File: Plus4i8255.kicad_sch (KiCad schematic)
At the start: 13 parts, among them CN1 EXPANSION_PORT, CN3 PIN_HEADER_32PIN, U1 8255, U2 GAL20V8

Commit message: TurboFloppy -> Plus4i8255
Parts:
- CN1: footprint TurboFloppy:C16_Cart_Conn -> Plus4i8255:C16_Cart_Conn
- V0: footprint TurboFloppy:cc_by_nc_sa -> Plus4i8255:cc_by_nc_sa
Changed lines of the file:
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@@
 			)
 		)
-		(property "Footprint" "TurboFloppy:cc_by_nc_sa"
+		(property "Footprint" "Plus4i8255:cc_by_nc_sa"
 			(at 128.27 193.04 0)
 			(effects
@@
 		)
 		(instances
-			(project "TurboFloppy"
+			(project "Plus4i8255"
 				(path "/0a31112a-e046-4d46-8b9e-0685d05e37f7"
 					(reference "#PWR011")
@@
 		)
 		(instances
-			(project "TurboFloppy"
+			(project "Plus4i8255"
 				(path "/0a31112a-e046-4d46-8b9e-0685d05e37f7"
 					(reference "#PWR026")
@@
 		)
 		(instances
-			(project "TurboFloppy"
+			(project "Plus4i8255"
 				(path "/0a31112a-e046-4d46-8b9e-0685d05e37f7"
 					(reference "#PWR07")
@@
 		)
 		(instances
-			(project "TurboFloppy"
+			(project "Plus4i8255"
 				(path "/0a31112a-e046-4d46-8b9e-0685d05e37f7"
 					(reference "#PWR028")
@@
 		)
 		(instances
-			(project "TurboFloppy"
+			(project "Plus4i8255"
 				(path "/0a31112a-e046-4d46-8b9e-0685d05e37f7"
 					(reference "#PWR023")
@@
 		)
 		(instances
-			(project "TurboFloppy"
+			(project "Plus4i8255"
 				(path "/0a31112a-e046-4d46-8b9e-0685d05e37f7"
 					(reference "#PWR019")
@@
 		)
 		(instances
-			(project "TurboFloppy"
+			(project "Plus4i8255"
 				(path "/0a31112a-e046-4d46-8b9e-0685d05e37f7"
 					(reference "#PWR06")
@@
 		)
 		(instances
-			(project "TurboFloppy"
+			(project "Plus4i8255"
 				(path "/0a31112a-e046-4d46-8b9e-0685d05e37f7"
 					(reference "C2")
@@
 		)
 		(instances
-			(project "TurboFloppy"
+			(project "Plus4i8255"
 				(path "/0a31112a-e046-4d46-8b9e-0685d05e37f7"
 					(reference "#PWR024")
@@
 		)
 		(instances
-			(project "TurboFloppy"
+			(project "Plus4i8255"
 				(path "/0a31112a-e046-4d46-8b9e-0685d05e37f7"
 					(reference "#PWR010")
@@
 		)
 		(instances
-			(project "TurboFloppy"
+			(project "Plus4i8255"
 				(path "/0a31112a-e046-4d46-8b9e-0685d05e37f7"
 					(reference "H2")
@@
 		)
 		(instances
-			(project "TurboFloppy"
+			(project "Plus4i8255"
 				(path "/0a31112a-e046-4d46-8b9e-0685d05e37f7"
 					(reference "#PWR09")
@@
 		)
 		(instances
-			(project "TurboFloppy"
+			(project "Plus4i8255"
 				(path "/0a31112a-e046-4d46-8b9e-0685d05e37f7"
 					(reference "RN3")
@@
 		)
 		(instances
-			(project "TurboFloppy"
+			(project "Plus4i8255"
 				(path "/0a31112a-e046-4d46-8b9e-0685d05e37f7"
 					(reference "RN2")
@@
 		)
 		(instances
-			(project "TurboFloppy"
+			(project "Plus4i8255"
 				(path "/0a31112a-e046-4d46-8b9e-0685d05e37f7"
 					(reference "#PWR04")
@@
 			)
 		)
-		(property "Footprint" "TurboFloppy:C16_Cart_Conn"
+		(property "Footprint" "Plus4i8255:C16_Cart_Conn"
 			(at 52.07 115.57 0)
 			(effects
@@
 		)
 		(instances
-			(project "TurboFloppy"
+			(project "Plus4i8255"
 				(path "/0a31112a-e046-4d46-8b9e-0685d05e37f7"
 					(reference "#PWR025")
@@
 		)
 		(instances
-			(project "TurboFloppy"
+			(project "Plus4i8255"
 				(path "/0a31112a-e046-4d46-8b9e-0685d05e37f7"
 					(reference "#PWR022")
@@
 		)
 		(instances
-			(project "TurboFloppy"
+			(project "Plus4i8255"
 				(path "/0a31112a-e046-4d46-8b9e-0685d05e37f7"
 					(reference "C1")
@@
 		)
 		(instances
-			(project "TurboFloppy"
+			(project "Plus4i8255"
 				(path "/0a31112a-e046-4d46-8b9e-0685d05e37f7"
 					(reference "#PWR03")
@@
 		)
 		(instances
-			(project "TurboFloppy"
+			(project "Plus4i8255"
 				(path "/0a31112a-e046-4d46-8b9e-0685d05e37f7"
 					(reference "#PWR05")
@@
 		)
 		(instances
-			(project "TurboFloppy"
+			(project "Plus4i8255"
 				(path "/0a31112a-e046-4d46-8b9e-0685d05e37f7"
 					(reference "#PWR027")
@@
 		)
 		(instances
-			(project "TurboFloppy"
+			(project "Plus4i8255"
 				(path "/0a31112a-e046-4d46-8b9e-0685d05e37f7"
 					(reference "#PWR020")
@@
 		)
 		(instances
-			(project "TurboFloppy"
+			(project "Plus4i8255"
 				(path "/0a31112a-e046-4d46-8b9e-0685d05e37f7"
 					(reference "#PWR08")

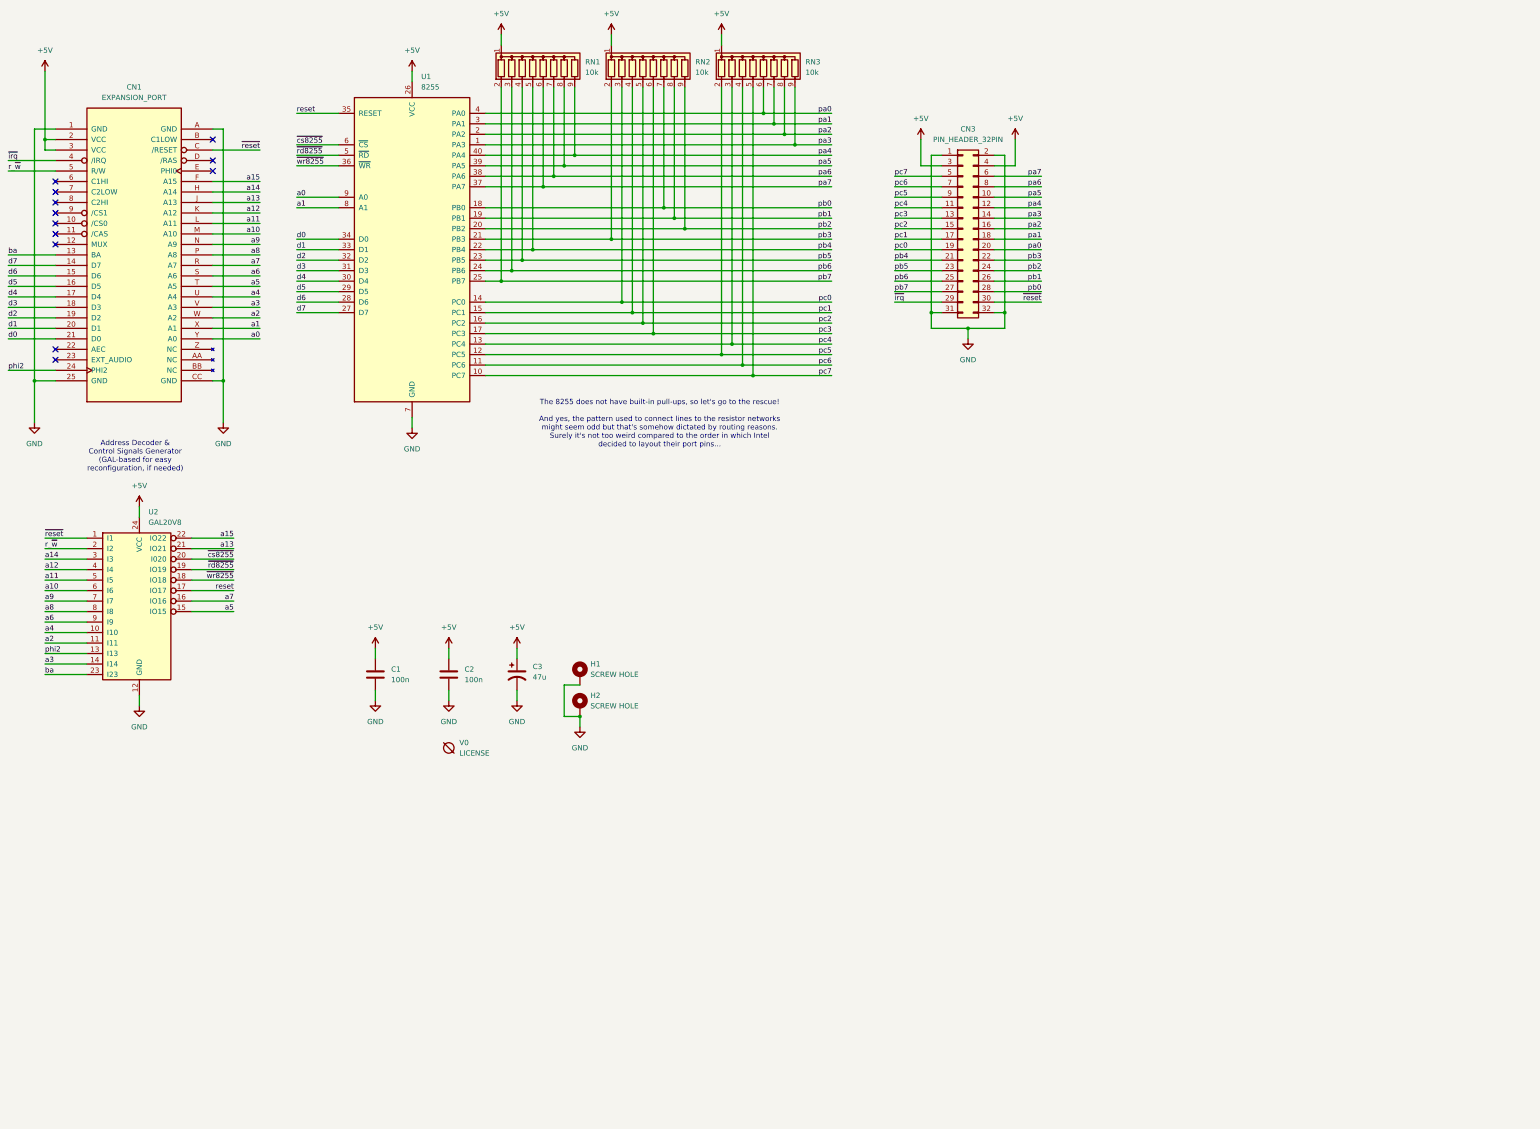
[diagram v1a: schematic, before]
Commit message: Add PC-style DB25 parallel port Inspired by zx_spectrum_parallel_interface by @msolajic TBD: Check DB25 footprint!
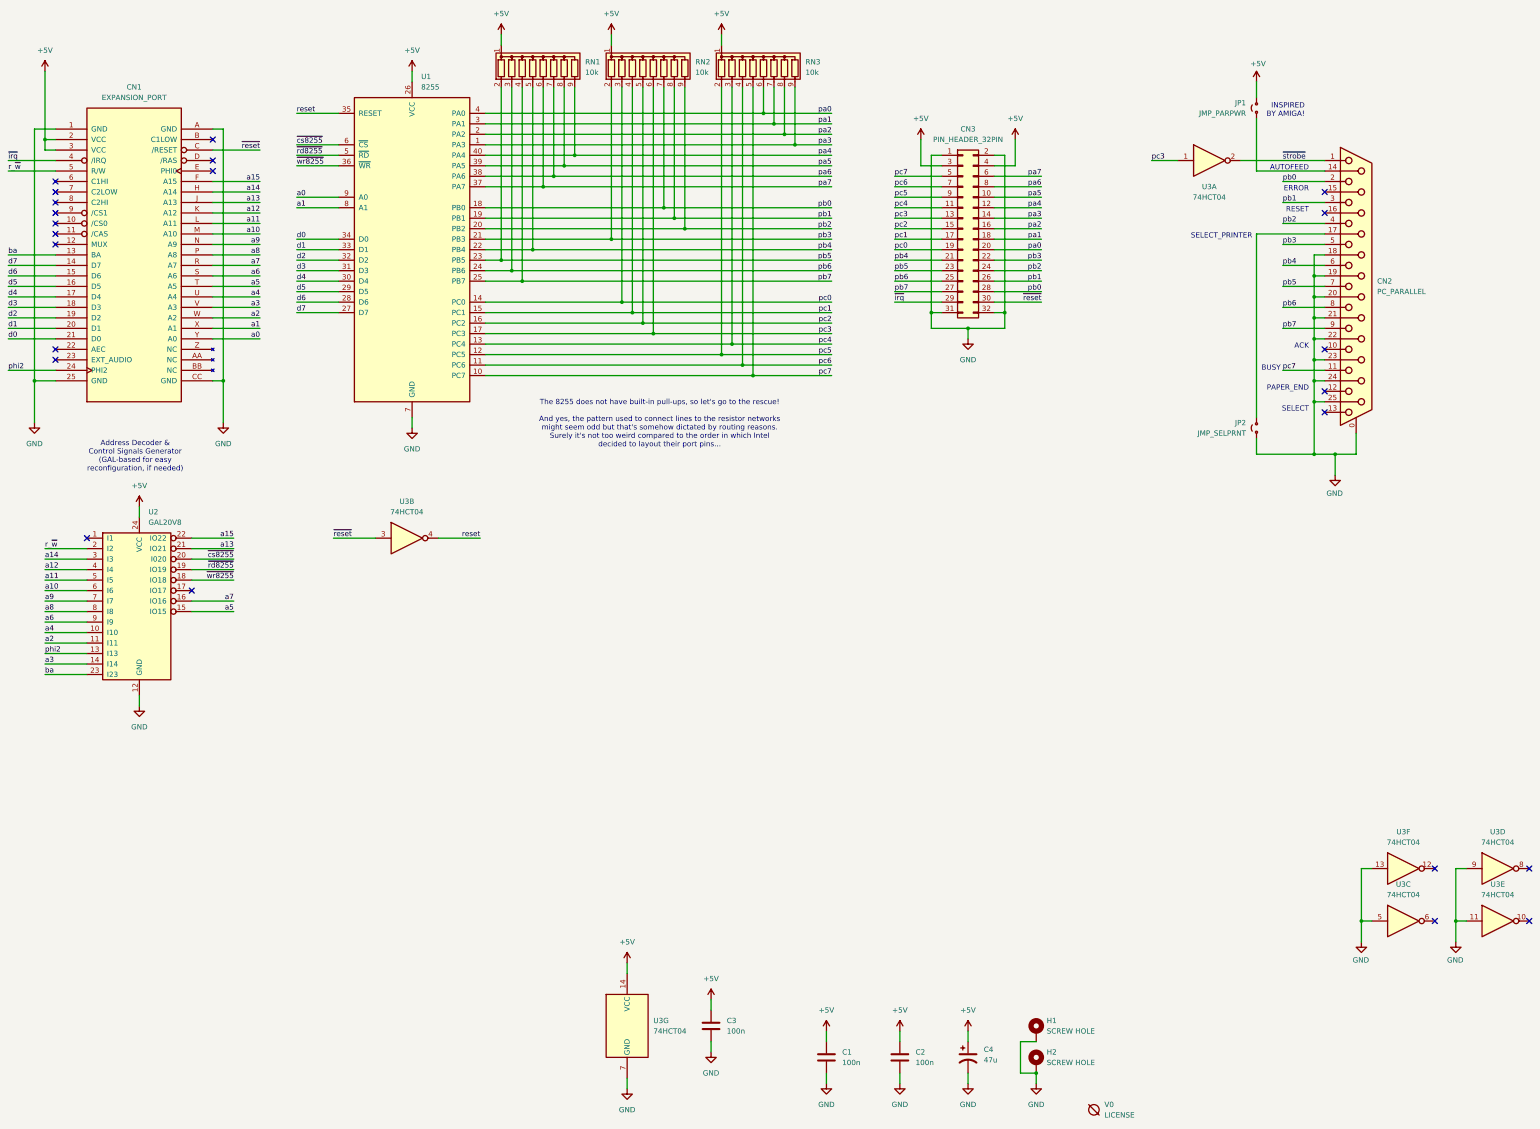
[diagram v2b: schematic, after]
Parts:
- added C3: 100n, Capacitor_THT:C_Disc_D7.0mm_W2.5mm_P5.00mm, symbol Device:C
- added CN2: PC_PARALLEL, Connector_Dsub:DSUB-25_Female_Horizontal_P2.77x2.84mm_EdgePinOffset7.70mm_Housed_MountingHolesOffset9.12mm, symbol Connector:DB25_Receptacle_MountingHoles
- added JP1: JMP_PARPWR, Jumper:SolderJumper-2_P1.3mm_Open_RoundedPad1.0x1.5mm, symbol Jumper:Jumper_2_Small_Open
- added JP2: JMP_SELPRNT, Jumper:SolderJumper-2_P1.3mm_Open_RoundedPad1.0x1.5mm, symbol Jumper:Jumper_2_Small_Open
- added U3: 74HCT04, Package_DIP:DIP-14_W7.62mm_Socket_LongPads, symbol 74xx:74HCT04
- renumbered C3 to C4
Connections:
- net +5V: now also C3.1, JP1.2 (B), U3.14 (VCC)
- net GND: now also C3.2, CN2.0 (PAD), CN2.18 (P18), CN2.19 (P19), CN2.20 (P20), CN2.21 (P21), CN2.22 (P22), CN2.23 (P23), CN2.24 (P24), CN2.25 (P25), JP2.1 (A), U3.11, U3.13, U3.5, U3.7 (GND), U3.9
- net pb0: now also CN2.2
- net pb1: now also CN2.3
- net pb2: now also CN2.4
- net pb3: now also CN2.5
- net pb4: now also CN2.6
- net pb5: now also RN1.2 (R1), CN2.7; no longer RN1.4 (R3)
- net pb6: now also CN2.8
- net pb7: now also RN1.4 (R3), CN2.9; no longer RN1.2 (R1)
- net pc3: now also U3.1
- net pc7: now also CN2.11
- net reset: now also U3.4; no longer U2.17 (IO17)
- net ~{reset}: now also U3.3; no longer U2.1 (I1)
- new net: CN2.17 (P17), JP2.2 (B)
- new net: CN2.14 (P14), JP1.1 (A)
- new net ~{strobe}: CN2.1, U3.2
- no-connect marks 12 -> 23
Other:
- note added: "ACK"
- note added: "AUTOFEED"
- note added: "BUSY"
- note added: "ERROR"
- note added: "INSPIRED BY AMIGA!"
- note added: "PAPER_END"
- note added: "RESET"
- note added: "SELECT"
- note added: "SELECT_PRINTER"
- moved on the sheet: C1, C2, C4, H1, H2, V0

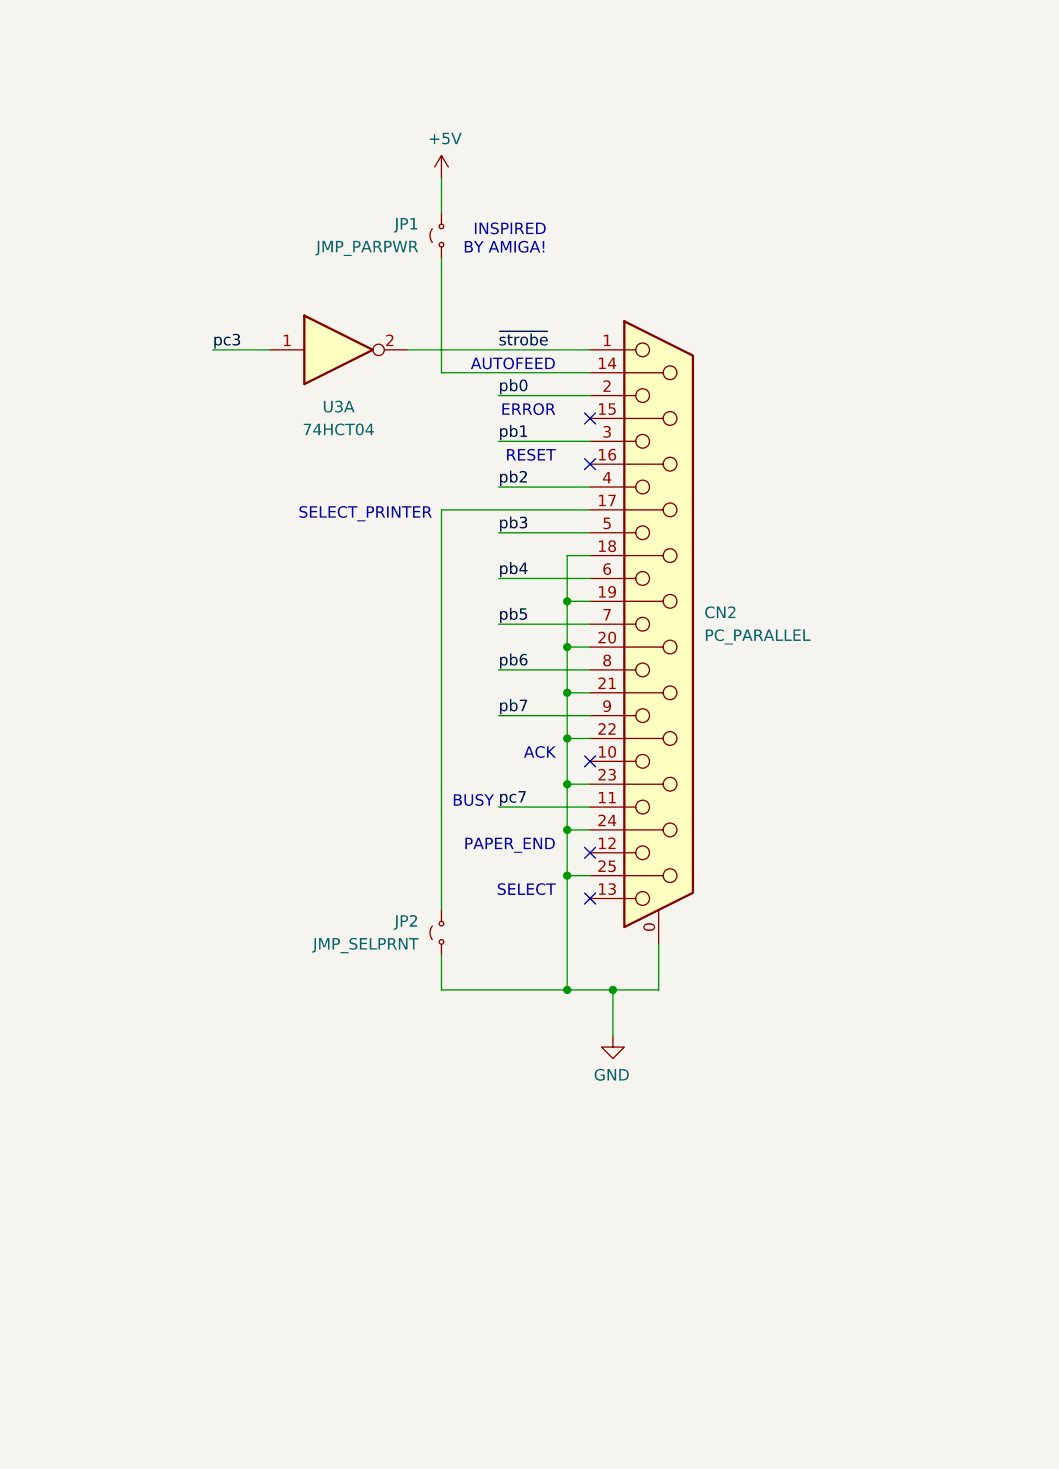
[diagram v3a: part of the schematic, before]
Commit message: Change pins of PC-style parallel port, hopefully adding potential bidirectional capability
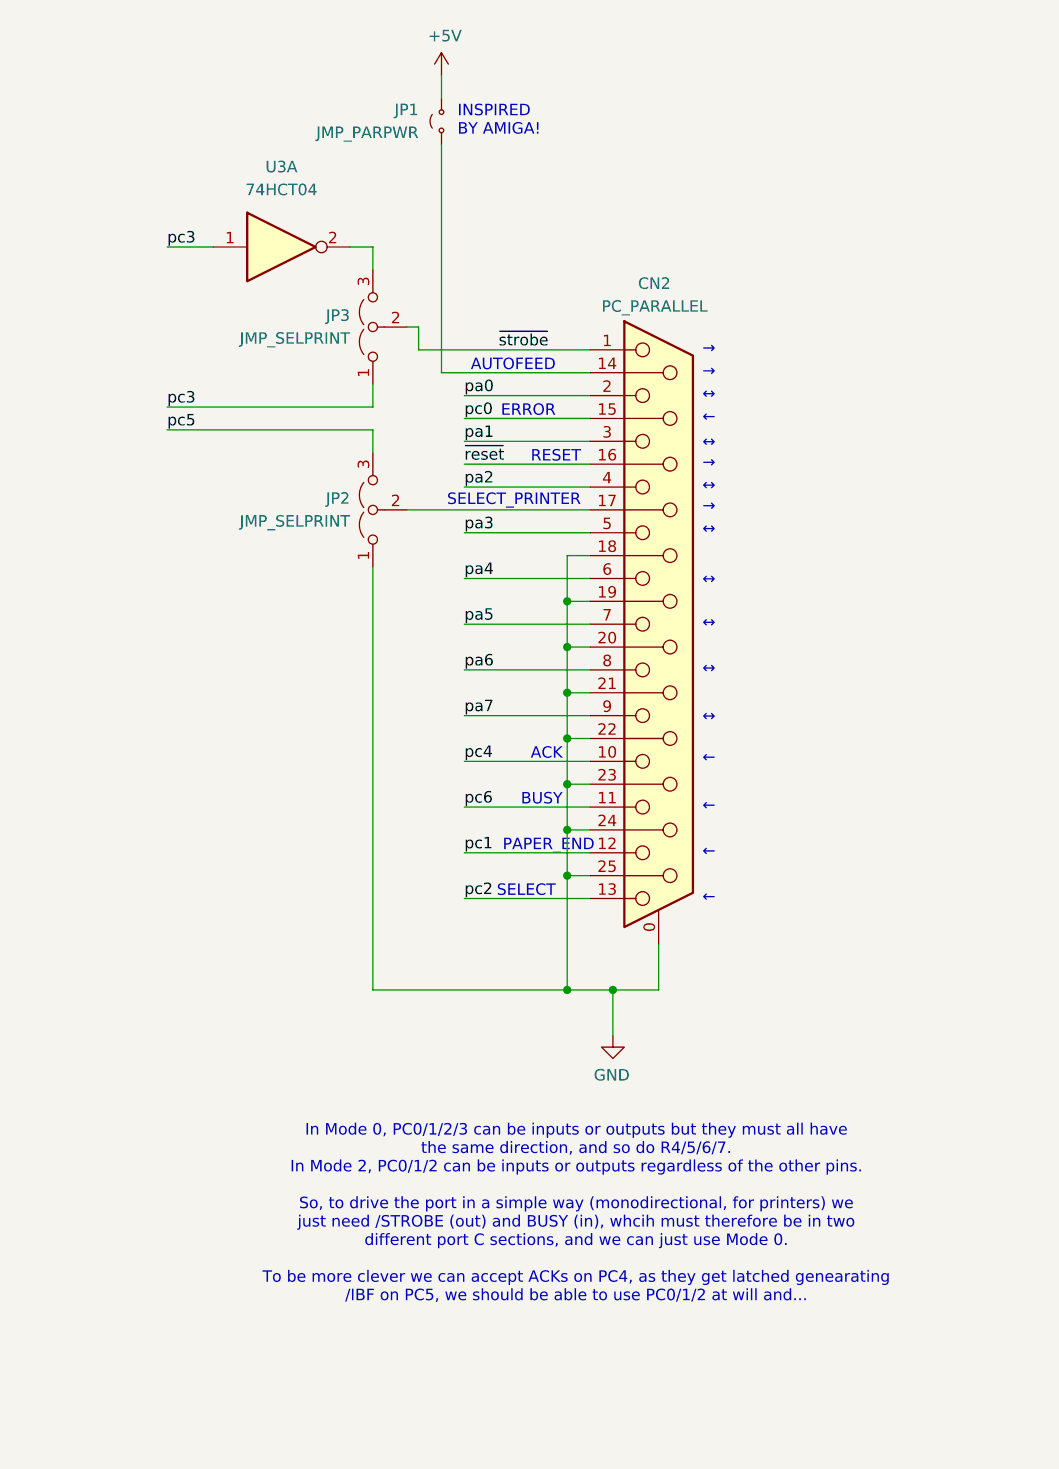
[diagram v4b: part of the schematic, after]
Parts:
- removed JP2: JMP_SELPRNT, Jumper:SolderJumper-2_P1.3mm_Open_RoundedPad1.0x1.5mm, symbol Jumper:Jumper_2_Small_Open
- added JP2, JP3: JMP_SELPRINT, Jumper:SolderJumper-3_P1.3mm_Open_RoundedPad1.0x1.5mm, symbol Jumper:Jumper_3_Open
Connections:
- net GND: now also JP2.1 (A)
- net pa0: now also CN2.2
- net pa1: now also CN2.3
- net pa2: now also CN2.4
- net pa3: now also CN2.5
- net pa4: now also CN2.6
- net pa5: now also CN2.7
- net pa6: now also CN2.8
- net pa7: now also CN2.9
- net pb0: no longer CN2.2
- net pb1: no longer CN2.3
- net pb2: no longer CN2.4
- net pb3: no longer CN2.5
- net pb4: no longer CN2.6
- net pb5: no longer CN2.7
- net pb6: no longer CN2.8
- net pb7: no longer CN2.9
- net pc0: now also CN2.15 (P15)
- net pc1: now also CN2.12
- net pc2: now also CN2.13
- net pc3: now also JP3.1 (A)
- net pc4: now also CN2.10
- net pc5: now also JP2.3 (B)
- net pc6: now also CN2.11
- net pc7: no longer CN2.11
- net ~{reset}: now also CN2.16 (P16)
- net ~{strobe}: now also JP3.2 (C); no longer U3.2
- net at CN2.17 (P17): now also JP2.2 (C)
- new net: JP3.3 (B), U3.2
- no-connect marks 23 -> 18
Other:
- note added: "In Mode 0, PC0/1/2/3 can be inputs or outputs but they must all have the same direction, and so do R4/5/6/7. In Mode 2, PC0/1/2 can be inputs or outputs regardless of the other pins. So, to drive the port in a simple way (monodirectional, for printers) we just need /STROBE (out) and BUSY (in), whcih must therefore be in two different port C sections, and we can just use Mode 0. To be more clever 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"
- note added: "←"
- note added: "→"
- note added: "↔"
- moved on the sheet: JP1, U3A
